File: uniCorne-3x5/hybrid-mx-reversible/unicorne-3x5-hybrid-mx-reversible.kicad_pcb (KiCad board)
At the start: 2 copper layers, 114.7 x 91.4 mm, 87 parts, among them J1 MJ-4PP-9, J2 Nice!View, J3 Conn_01x02, J4 Conn_01x03, SW1 SW_MX_HS, SW10 SW_MX_HS, SW11 SW_MX_HS, SW12 SW_MX_HS, SW13 SW_MX_HS, SW14 SW_MX_HS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

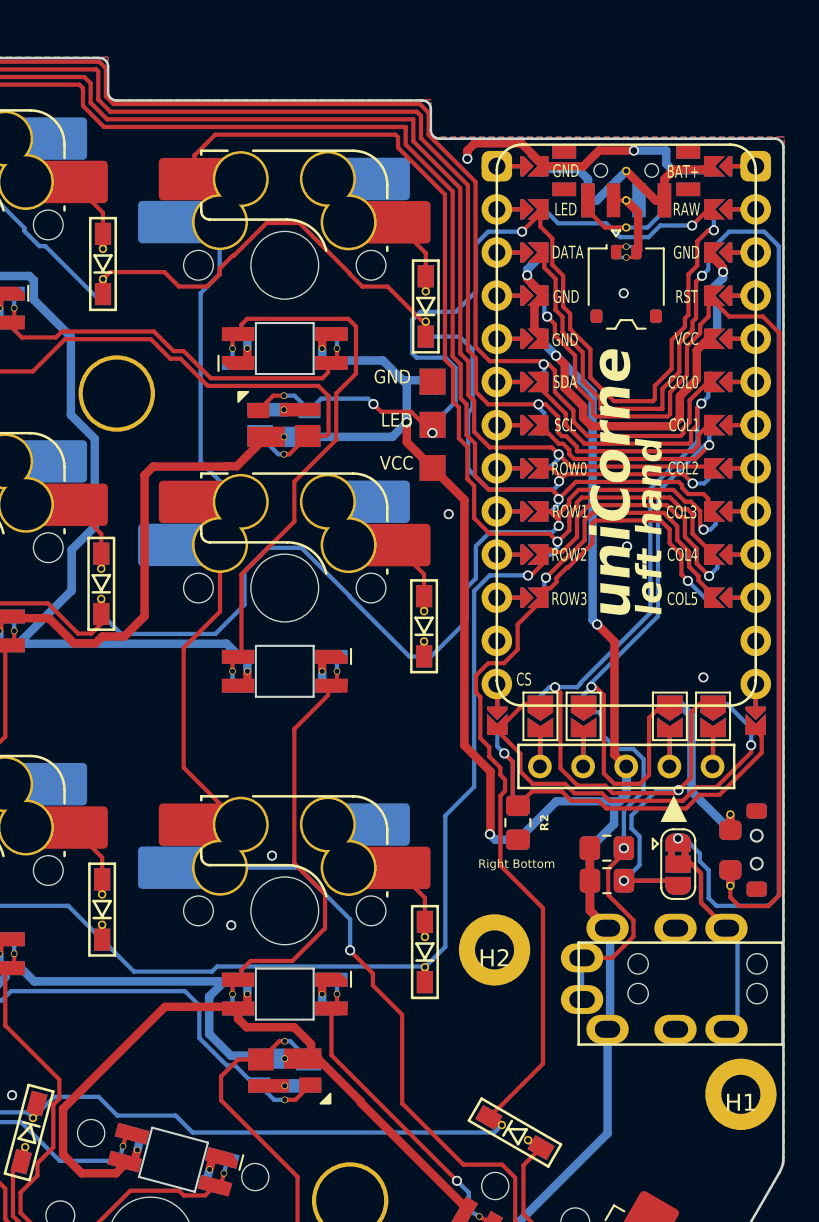
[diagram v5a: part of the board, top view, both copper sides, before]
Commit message: fixed 3x5 hyprid mx
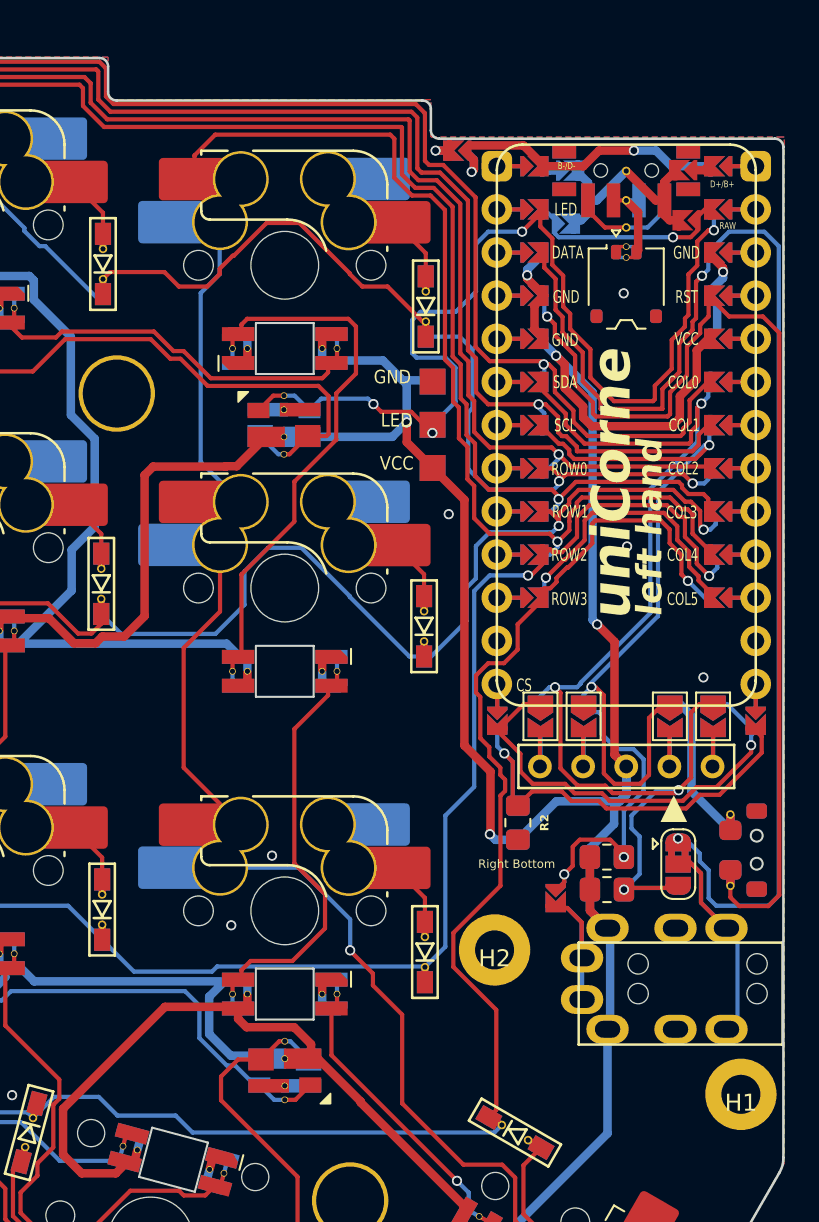
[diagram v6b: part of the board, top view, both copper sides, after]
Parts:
- added JP10: , TB2086_MISC:SolderJumper-2_P1.3mm_Open_TrianglePad1.0x1.2mm_rev, F.Cu at (181.3, 112.8)
- added JP11: , TB2086_MISC:SolderJumper-2_P1.3mm_Open_TrianglePad1.0x1.2mm_rev, F.Cu at (175.5, 68.8)
- added JP12: , TB2086_MISC:SolderJumper-2_P1.3mm_Open_TrianglePad1.0x1.2mm, B.Cu at (182.2, 70.0)
- added JP13: , TB2086_MISC:SolderJumper-2_P1.3mm_Open_TrianglePad1.0x1.2mm, F.Cu at (188.8, 70.0)
- added JP14: , TB2086_MISC:SolderJumper-2_P1.3mm_Open_TrianglePad1.0x1.2mm, F.Cu at (189.0, 72.9)
- added JP15: , TB2086_MISC:SolderJumper-2_P1.3mm_Open_TrianglePad1.0x1.2mm, B.Cu at (181.9, 73.1)
- U1: footprint TB2086_MISC:ProMicro-ish-dn-rev-unrouted_3x6 -> TB2086_MISC:ProMicro-ish-dn-rev-unrouted_3x5
- moved R3 0.53 mm to (184.3, 110.4)
- moved R4 0.52 mm to (184.3, 112.3)
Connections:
- J1 pad A: SCL -> Net-(JP10-B)
- U1 pad 24: unconnected-(U1-RAW-Pad24) -> RAW
- U1 pad 25: BAT+ -> D+/B+
- U1 pad 26: GND -> B-/D-
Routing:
- net B-/D-: track 0.00 -> 18.2 mm, vias 0 -> 2
- net GND: track 38.3 -> 22.9 mm, vias 16 -> 15
- net RAW: track 0.00 -> 11.9 mm, vias 0 -> 1
- net unconnected-(U1-RAW-Pad24): track 11.0 -> 0.00 mm, vias 1 -> 0
- net Net-(JP10-B): track 0.00 -> 10.4 mm
- net SCL: track 66.1 -> 62.5 mm, vias 3 -> 4
- net D+/B+: track 0.00 -> 1.91 mm
- net SDA: track 69.8 -> 70.8 mm
- net BAT+: track 14.2 -> 13.4 mm
- net VCC: track 501.4 -> 500.8 mm
